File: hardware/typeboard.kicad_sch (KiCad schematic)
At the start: 69 parts, among them J2 AXK6F20347YG

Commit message: :sparkles: assembly all the part!
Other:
- moved on the sheet: J2, LED1, LED10, LED11, LED12, LED13, LED14, LED15, LED16, LED17, LED18, LED19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

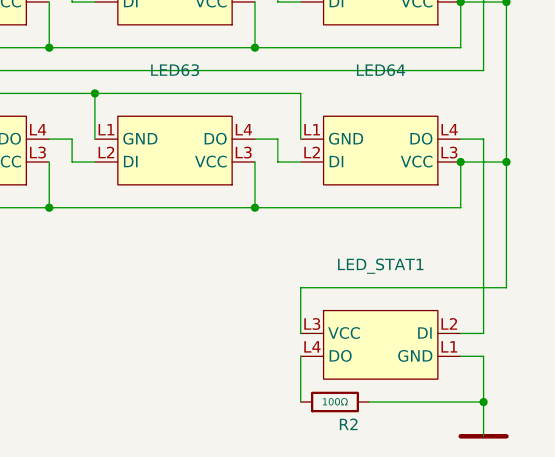
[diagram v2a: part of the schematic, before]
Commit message: :art: improve LED positions
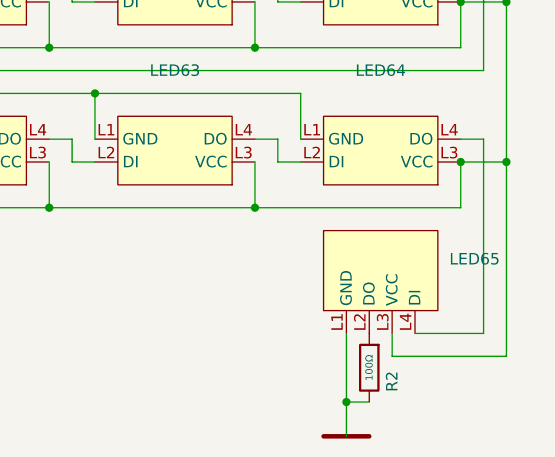
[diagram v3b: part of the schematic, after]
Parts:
- removed LED_STAT1: ~, KeysDock:XL-3528RGBW-WS2812B, symbol components:XL-3528RGBW-WS2812B
- added LED65: ~, KeysDock:XL-3512RGBW-WS2812B, symbol components:XL-3512RGBW-WS2812B
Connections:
- net P,+5: now also LED65.L3 (VCC)
- net P,E: now also LED65.L1 (GND)
- net at LED64.L4 (DO): now also LED65.L4 (DI)
- net at R2.1: now also LED65.L2 (DO)
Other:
- moved on the sheet: R2

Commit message: :sparkles: add bom table
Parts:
- J2: LCSC (none) -> C559781; Manufacturer (none) -> Panasonic; PartNumber (none) -> AXK6F20347YG
- LED1, LED10, LED11, LED12, LED13, LED14, LED15, LED16, LED17, LED18, LED19, LED2, LED20, LED21, LED22, LED23, LED24, LED25, LED26, LED27, LED28, LED29, LED3, LED30, LED31, LED32, LED33, LED34, LED35, LED36, LED37, LED38, LED39, LED4, LED40, LED41, LED42, LED43, LED44, LED45, LED46, LED47, LED48, LED49, LED5, LED50, LED51, LED52, LED53, LED54, LED55, LED56, LED57, LED58, LED59, LED6, LED60, LED61, LED62, LED63, LED64, LED7, LED8, LED9: value ~ -> XL-6028RGBW-WS2812B; LCSC (none) -> C42163197; Manufacturer (none) -> XINGLIGHT(成兴光)
- LED65: value ~ -> XL-3512RGBW-WS2812B; LCSC (none) -> C49237874; Manufacturer (none) -> XINGLIGHT(成兴光)

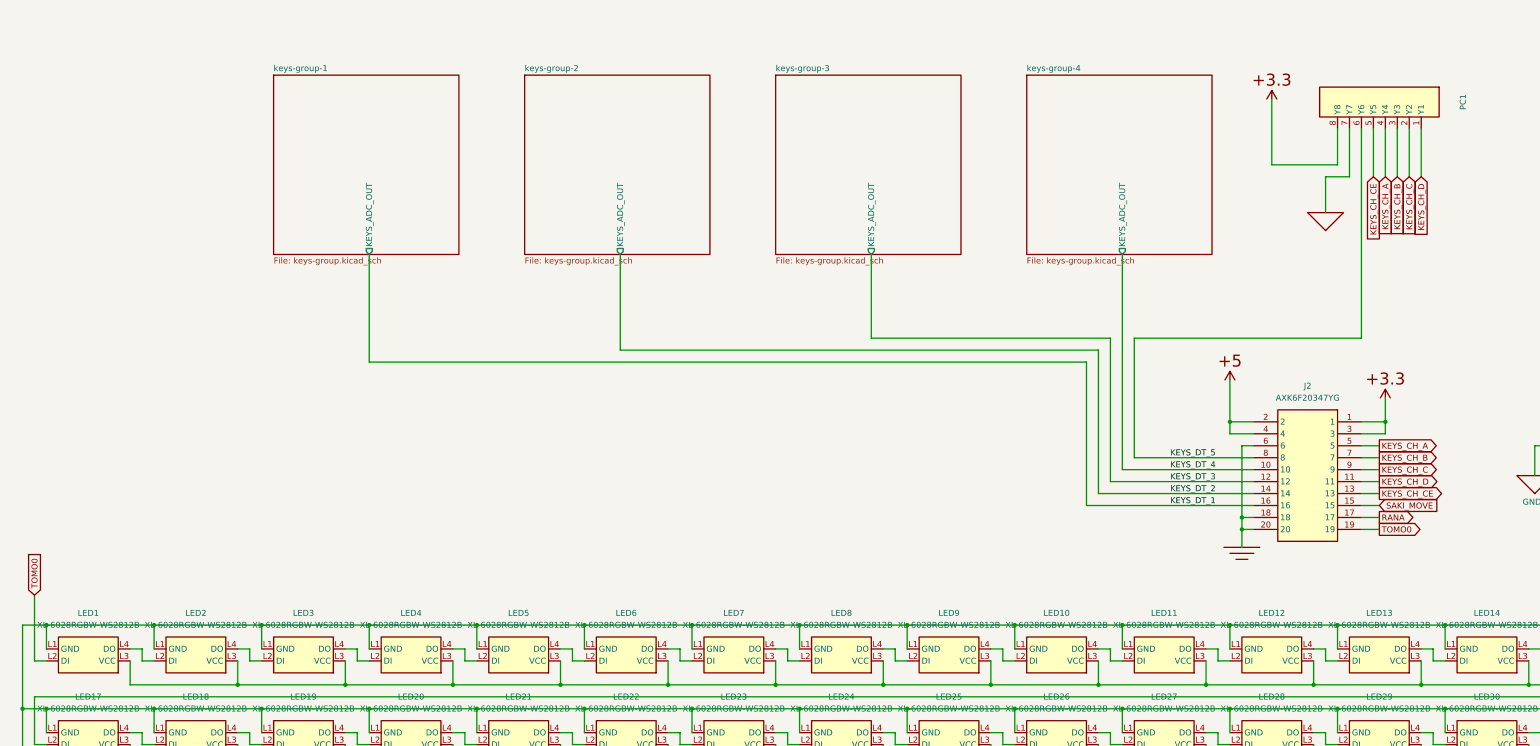
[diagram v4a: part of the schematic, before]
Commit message: :construction: panelize all boards
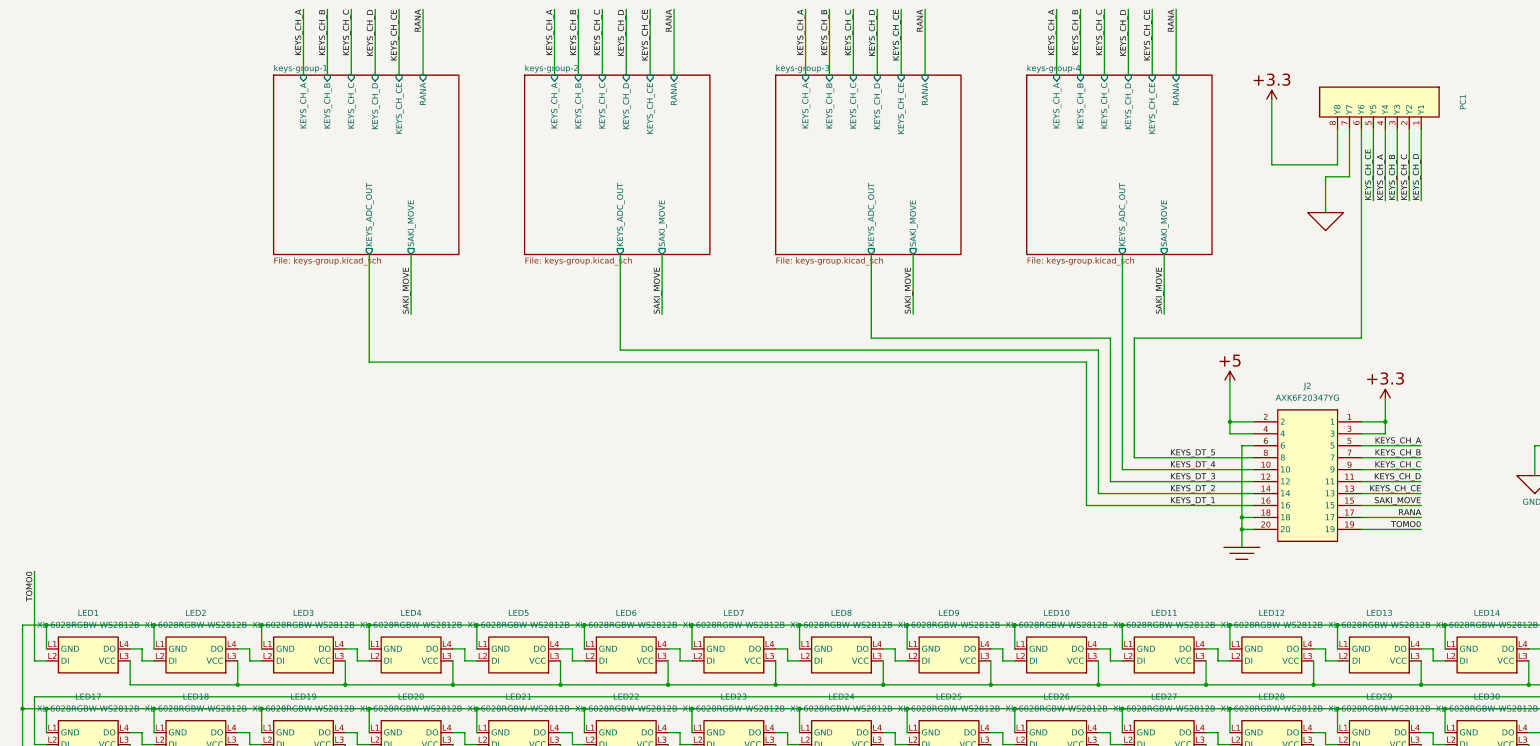
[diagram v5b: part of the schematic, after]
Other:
- sheet keys-group-1 ports: added KEYS_CH_A, KEYS_CH_B, KEYS_CH_C, KEYS_CH_CE, KEYS_CH_D, RANA, SAKI_MOVE; removed none
- sheet keys-group-2 ports: added KEYS_CH_A, KEYS_CH_B, KEYS_CH_C, KEYS_CH_CE, KEYS_CH_D, RANA, SAKI_MOVE; removed none
- sheet keys-group-3 ports: added KEYS_CH_A, KEYS_CH_B, KEYS_CH_C, KEYS_CH_CE, KEYS_CH_D, RANA, SAKI_MOVE; removed none
- sheet keys-group-4 ports: added KEYS_CH_A, KEYS_CH_B, KEYS_CH_C, KEYS_CH_CE, KEYS_CH_D, RANA, SAKI_MOVE; removed none
